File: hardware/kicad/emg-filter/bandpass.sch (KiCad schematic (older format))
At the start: 88 parts, among them U12 LM4565

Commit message: fixed rect labels
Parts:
- gave numbers to parts that had none: 79
- renumbered C19 to C78, C20 to C79, C28 to C84, C25 to C85, R43 to R40, R44 to R41, R52 to R46, R49 to R47, U12 to U11

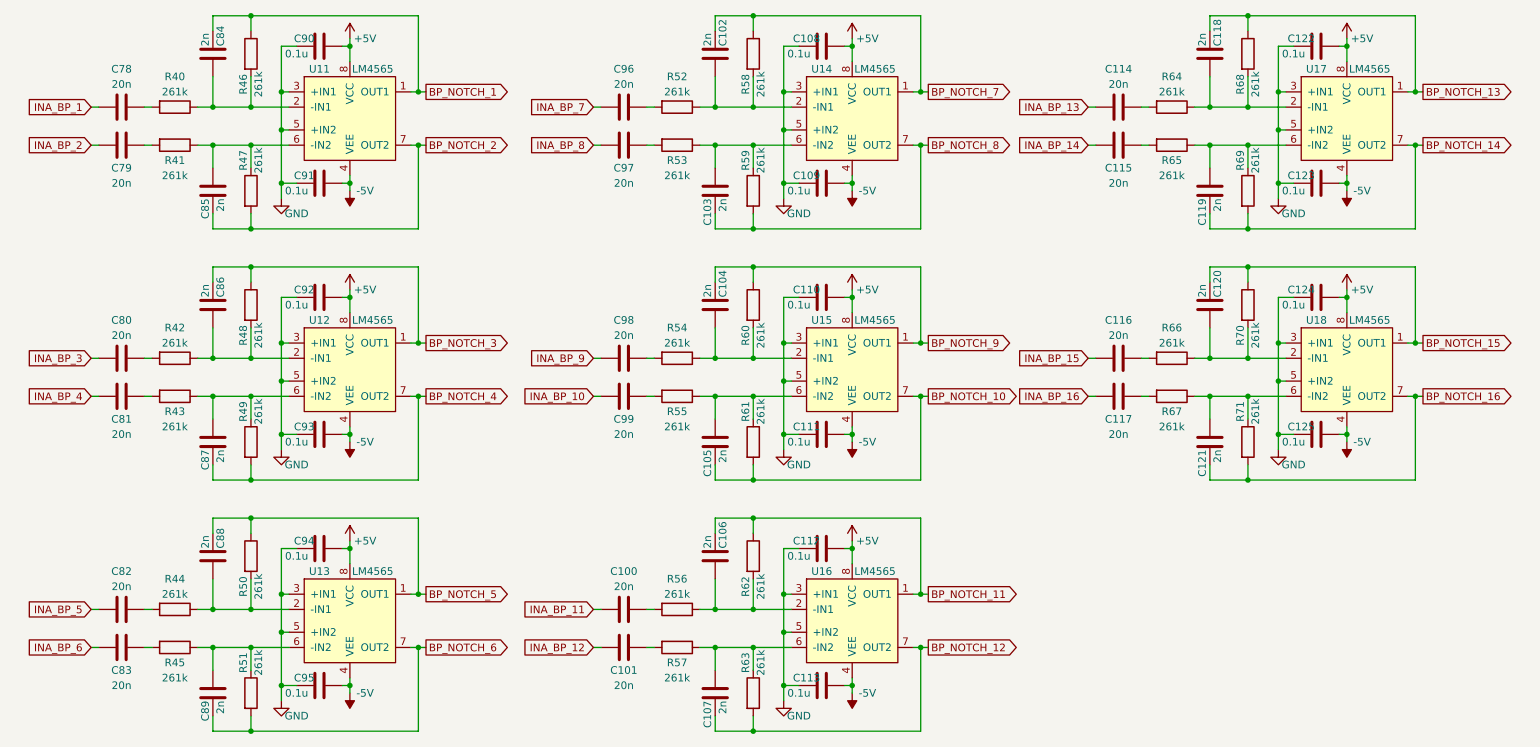
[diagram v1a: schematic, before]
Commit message: footprint association
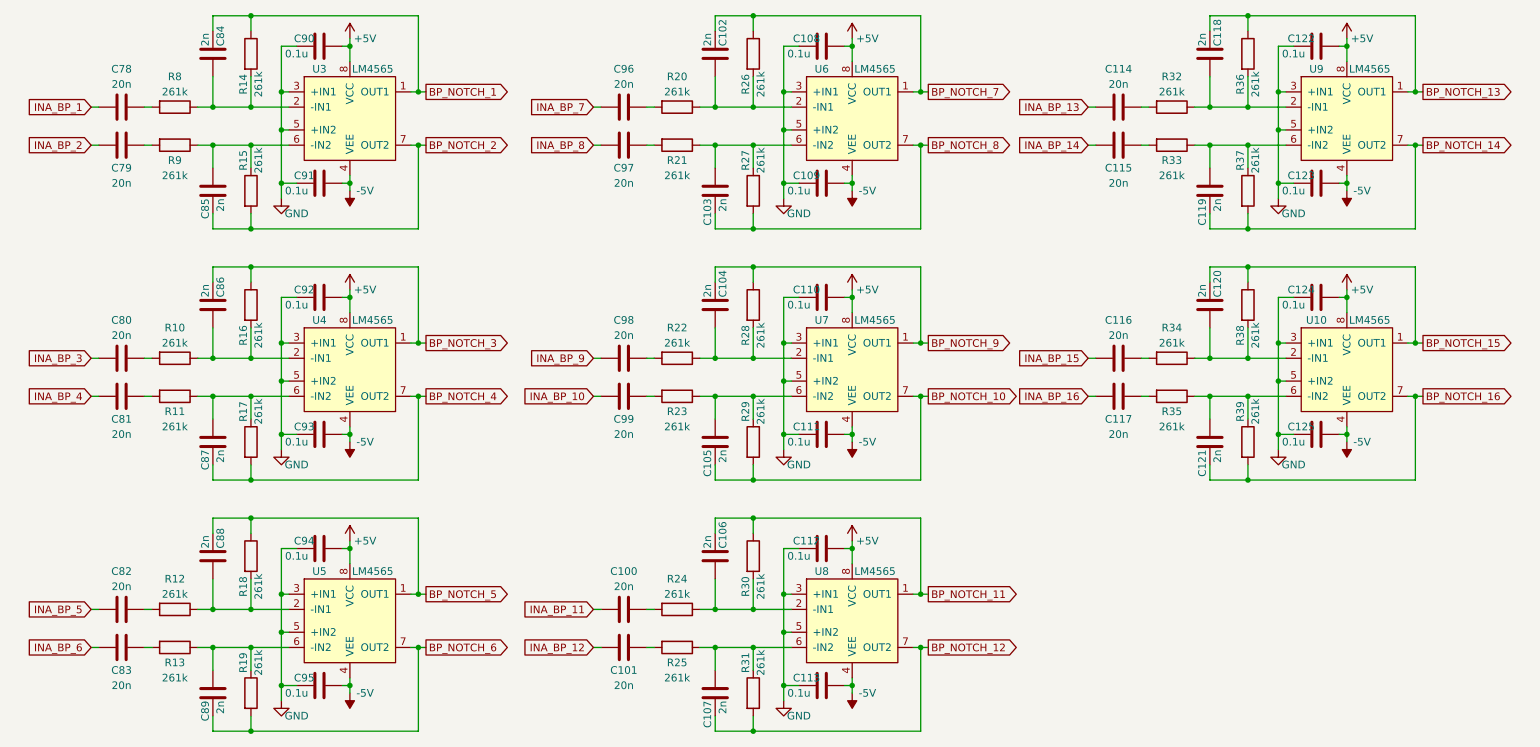
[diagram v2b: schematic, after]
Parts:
- C100, C101, C102, C103, C104, C105, C106, C107, C108, C109, C110, C111, C112, C113, C114, C115, C116, C117, C118, C119, C120, C121, C122, C123, C124, C125, C78, C79, C80, C81, C82, C83, C84, C85, C86, C87, C88, C89, C90, C91, C92, C93, C94, C95, C96, C97, C98, C99: footprint (none) -> Capacitor_SMD:C_0805_2012Metric
- R10: renamed from R42; footprint (none) -> Resistor_SMD:R_0805_2012Metric
- R11: renamed from R43; footprint (none) -> Resistor_SMD:R_0805_2012Metric
- R12: renamed from R44; footprint (none) -> Resistor_SMD:R_0805_2012Metric
- R13: renamed from R45; footprint (none) -> Resistor_SMD:R_0805_2012Metric
- R14: renamed from R46; footprint (none) -> Resistor_SMD:R_0805_2012Metric
- R15: renamed from R47; footprint (none) -> Resistor_SMD:R_0805_2012Metric
- R16: renamed from R48; footprint (none) -> Resistor_SMD:R_0805_2012Metric
- R17: renamed from R49; footprint (none) -> Resistor_SMD:R_0805_2012Metric
- R18: renamed from R50; footprint (none) -> Resistor_SMD:R_0805_2012Metric
- R19: renamed from R51; footprint (none) -> Resistor_SMD:R_0805_2012Metric
- R20: renamed from R52; footprint (none) -> Resistor_SMD:R_0805_2012Metric
- R21: renamed from R53; footprint (none) -> Resistor_SMD:R_0805_2012Metric
- R22: renamed from R54; footprint (none) -> Resistor_SMD:R_0805_2012Metric
- R23: renamed from R55; footprint (none) -> Resistor_SMD:R_0805_2012Metric
- R24: renamed from R56; footprint (none) -> Resistor_SMD:R_0805_2012Metric
- R25: renamed from R57; footprint (none) -> Resistor_SMD:R_0805_2012Metric
- R26: renamed from R58; footprint (none) -> Resistor_SMD:R_0805_2012Metric
- R27: renamed from R59; footprint (none) -> Resistor_SMD:R_0805_2012Metric
- R28: renamed from R60; footprint (none) -> Resistor_SMD:R_0805_2012Metric
- R29: renamed from R61; footprint (none) -> Resistor_SMD:R_0805_2012Metric
- R30: renamed from R62; footprint (none) -> Resistor_SMD:R_0805_2012Metric
- R31: renamed from R63; footprint (none) -> Resistor_SMD:R_0805_2012Metric
- R32: renamed from R64; footprint (none) -> Resistor_SMD:R_0805_2012Metric
- R33: renamed from R65; footprint (none) -> Resistor_SMD:R_0805_2012Metric
- R34: renamed from R66; footprint (none) -> Resistor_SMD:R_0805_2012Metric
- R35: renamed from R67; footprint (none) -> Resistor_SMD:R_0805_2012Metric
- R36: renamed from R68; footprint (none) -> Resistor_SMD:R_0805_2012Metric
- R37: renamed from R69; footprint (none) -> Resistor_SMD:R_0805_2012Metric
- R38: renamed from R70; footprint (none) -> Resistor_SMD:R_0805_2012Metric
- R39: renamed from R71; footprint (none) -> Resistor_SMD:R_0805_2012Metric
- R8: renamed from R40; footprint (none) -> Resistor_SMD:R_0805_2012Metric
- R9: renamed from R41; footprint (none) -> Resistor_SMD:R_0805_2012Metric
- renumbered U18 to U10, U11 to U3, U12 to U4, U13 to U5, U14 to U6, U15 to U7, U16 to U8, U17 to U9
